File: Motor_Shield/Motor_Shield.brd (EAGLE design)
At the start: 62.2 x 53.3 mm, 28 parts, among them U1 MOCD213, U2 MOCD213, U3 MOCD213, U4 ARDUINO_SHIELDLABEL, X1 2510-, X2 2510-, X5 C-GRID-05-15-91, X6 C-GRID-05-15-91

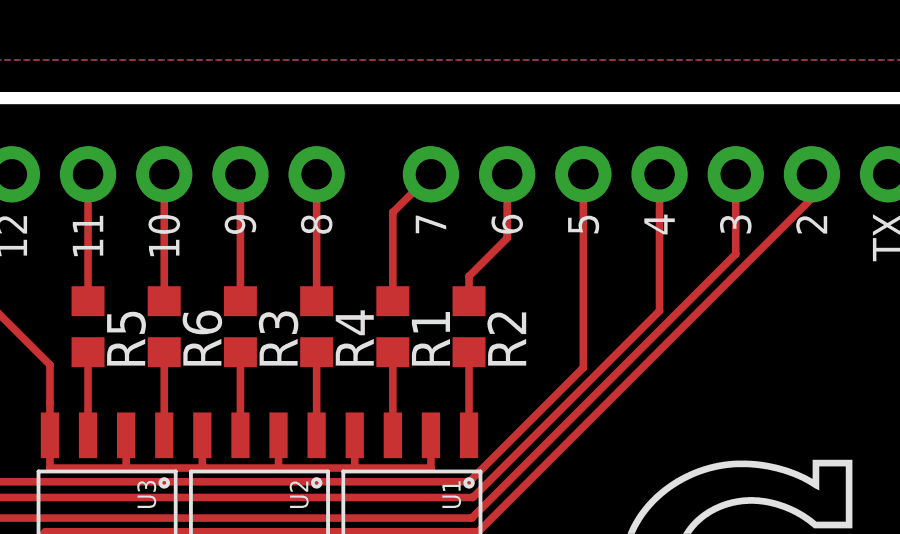
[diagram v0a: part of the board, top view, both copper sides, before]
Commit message: Edited modified board design, pinout fixed
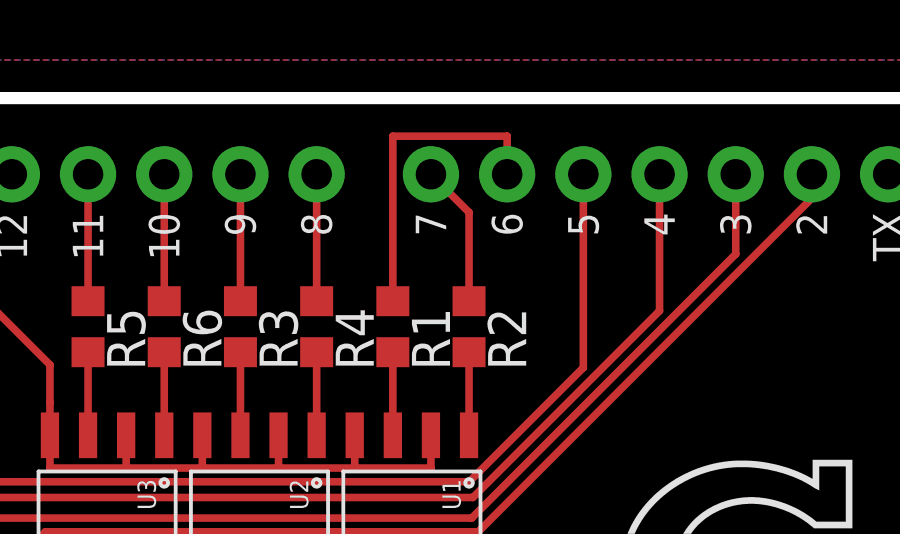
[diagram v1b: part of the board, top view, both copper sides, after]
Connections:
- net LEFT_DIRECTION: now also U4.D7; no longer U4.D6
- net LEFT_SPEED: now also U4.D6; no longer U4.D7
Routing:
- net LEFT_SPEED: track 4.76 -> 10.6 mm
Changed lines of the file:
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@@
 <?xml version="1.0" encoding="utf-8"?>
 <!DOCTYPE eagle SYSTEM "eagle.dtd">
-<eagle version="6.4">
+<eagle version="7.4.0">
 <drawing>
 <settings>
@@
 <pass name="Default">
 <param name="RoutingGrid" value="50mil"/>
+<param name="AutoGrid" value="1"/>
+<param name="Efforts" value="0"/>
+<param name="TopRouterVariant" value="1"/>
 <param name="tpViaShape" value="round"/>
 <param name="PrefDir.1" value="|"/>
@@
 </signal>
 <signal name="LEFT_SPEED">
-<contactref element="U4" pad="D7"/>
 <contactref element="R1" pad="1"/>
-<wire x1="36.83" y1="50.8" x2="35.56" y2="49.53" width="0.254" layer="1"/>
-<wire x1="35.56" y1="49.53" x2="35.56" y2="46.57" width="0.254" layer="1"/>
+<wire x1="35.56" y1="52.07" x2="35.56" y2="46.57" width="0.254" layer="1"/>
+<contactref element="U4" pad="D6"/>
+<wire x1="35.56" y1="52.07" x2="39.37" y2="52.07" width="0.254" layer="1"/>
+<wire x1="39.37" y1="52.07" x2="39.37" y2="50.8" width="0.254" layer="1"/>
 </signal>
 <signal name="GND">
@@
 </signal>
 <signal name="LEFT_DIRECTION">
-<contactref element="U4" pad="D6"/>
 <contactref element="R2" pad="1"/>
-<wire x1="38.1" y1="46.57" x2="38.1" y2="47.4003" width="0.254" layer="1"/>
-<wire x1="39.37" y1="50.8" x2="39.37" y2="48.6703" width="0.254" layer="1"/>
-<wire x1="39.37" y1="48.6703" x2="38.1" y2="47.4003" width="0.254" layer="1"/>
+<contactref element="U4" pad="D7"/>
+<wire x1="38.1" y1="46.57" x2="38.1" y2="49.53" width="0.254" layer="1"/>
+<wire x1="38.1" y1="49.53" x2="36.83" y2="50.8" width="0.254" layer="1"/>
 </signal>
 <signal name="RIGHT_BLI">
